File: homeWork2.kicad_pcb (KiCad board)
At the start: 2 copper layers, 125 x 99.9 mm, 43 parts, among them J1 Barrel_Jack_Switch_SMT, U1 LM7805_TO220

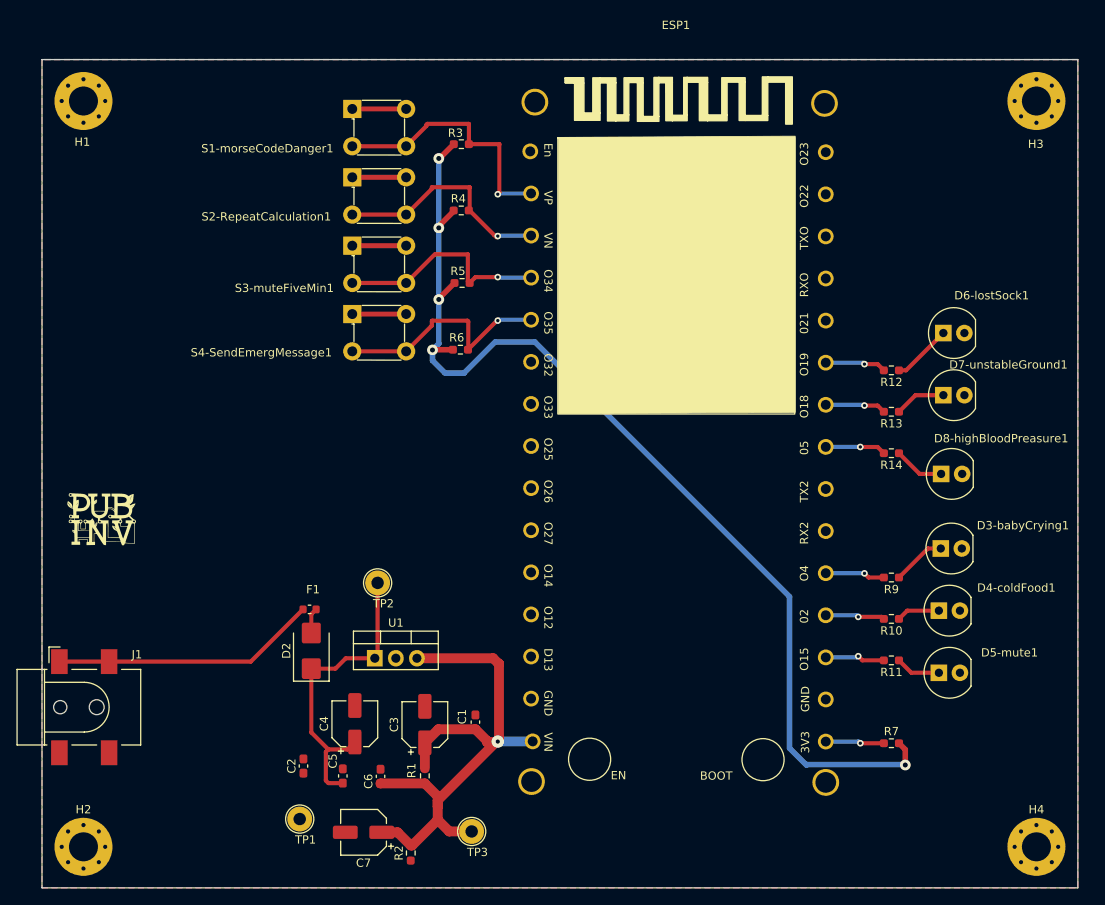
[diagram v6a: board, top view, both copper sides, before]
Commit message: capacitors are placed for high frequency and to minimize stray conductance. Classes are editted and a unique Net class is added for power and some net are renamed and assigned to it the suitable Net Class. For example, Vin PVRAW ESP1-3V3 and ESP1-5V are assgined to it PWR Net class.
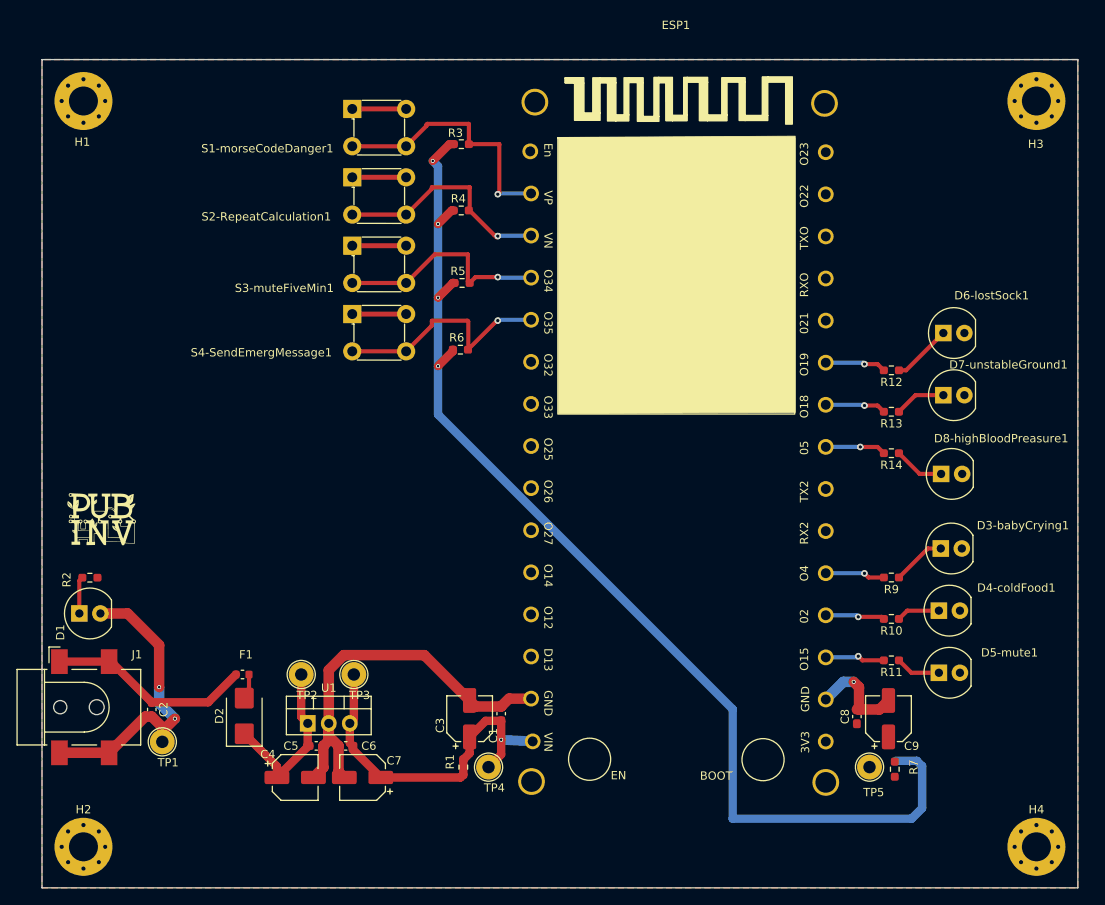
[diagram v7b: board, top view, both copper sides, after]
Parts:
- added C8: 100nF, Capacitor_SMD:C_0603_1608Metric_Pad1.08x0.95mm_HandSolder, F.Cu at (148.3, 129.3)
- added C9: 47uF 16V, Capacitor_SMD:CP_Elec_5x5.4, F.Cu at (152.1, 129.5)
- added D1: LED_T1.75_CLEAR_RED, GeneralPurposeAlarmDevicePCB:LED_5mm_Radial, F.Cu at (57.0, 116.8)
- added TP4: TestPoint, TestPoint:TestPoint_Loop_D2.54mm_Drill1.5mm_Beaded, F.Cu at (103.9, 135.4)
- added TP5: TestPoint, TestPoint:TestPoint_Loop_D2.54mm_Drill1.5mm_Beaded, F.Cu at (149.9, 135.4)
- R1: value R -> 1R
- R7: value 1 Ohm -> 1R
- moved R2 51.0 mm to (55.8, 112.5), turned to 0 degrees
- moved TP3 23.7 mm to (87.6, 124.2)
- moved C2 19.5 mm to (63.2, 128.4), turned to -90 degrees
- moved TP1 19.0 mm to (64.5, 132.3)
- moved TP2 14.4 mm to (81.3, 124.2)
- moved F1 11.3 mm to (74.2, 124.2)
- moved D2 11.3 mm to (74.4, 129.2)
- moved U1 11.3 mm to (82.1, 130.1)
- moved C4 9.69 mm to (80.6, 136.6), turned to 0 degrees
- moved C7 6.62 mm to (88.7, 136.6)
- moved C6 5.58 mm to (86.6, 132.8), turned to 180 degrees
- moved C3 5.45 mm to (101.6, 129.5)
- moved C5 4.84 mm to (83.1, 132.8), turned to 0 degrees
- moved R1 4.76 mm to (100.8, 135.4)
- moved C1 3.27 mm to (105.4, 128.9)
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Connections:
- C2 pad 1: GND -> /PVRAW
- F1 pad 2: Net-(F1-Pad2) -> /PVRAW
- J1 pad 1: Net-(F1-Pad2) -> /PVRAW
- J1 pad 4: Net-(F1-Pad2) -> /PVRAW
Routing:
- net GND: track 26.1 -> 125.6 mm, vias 0 -> 3
- net Net-(F1-Pad2): track 32.0 -> 0.00 mm
- net +5V: track 72.4 -> 43.8 mm
- net /PVRAW: track 0.00 -> 24.7 mm
- net Vin: track 37.6 -> 21.9 mm
- net +3.3V: track 129.0 -> 137.7 mm, vias 5 -> 4
- net Net-(ESP1-3V3): track 7.09 -> 0.00 mm, vias 1 -> 0
- net Net-(D1-Pad1): track 0.00 -> 4.47 mm
